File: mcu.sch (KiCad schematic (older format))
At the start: 8 parts

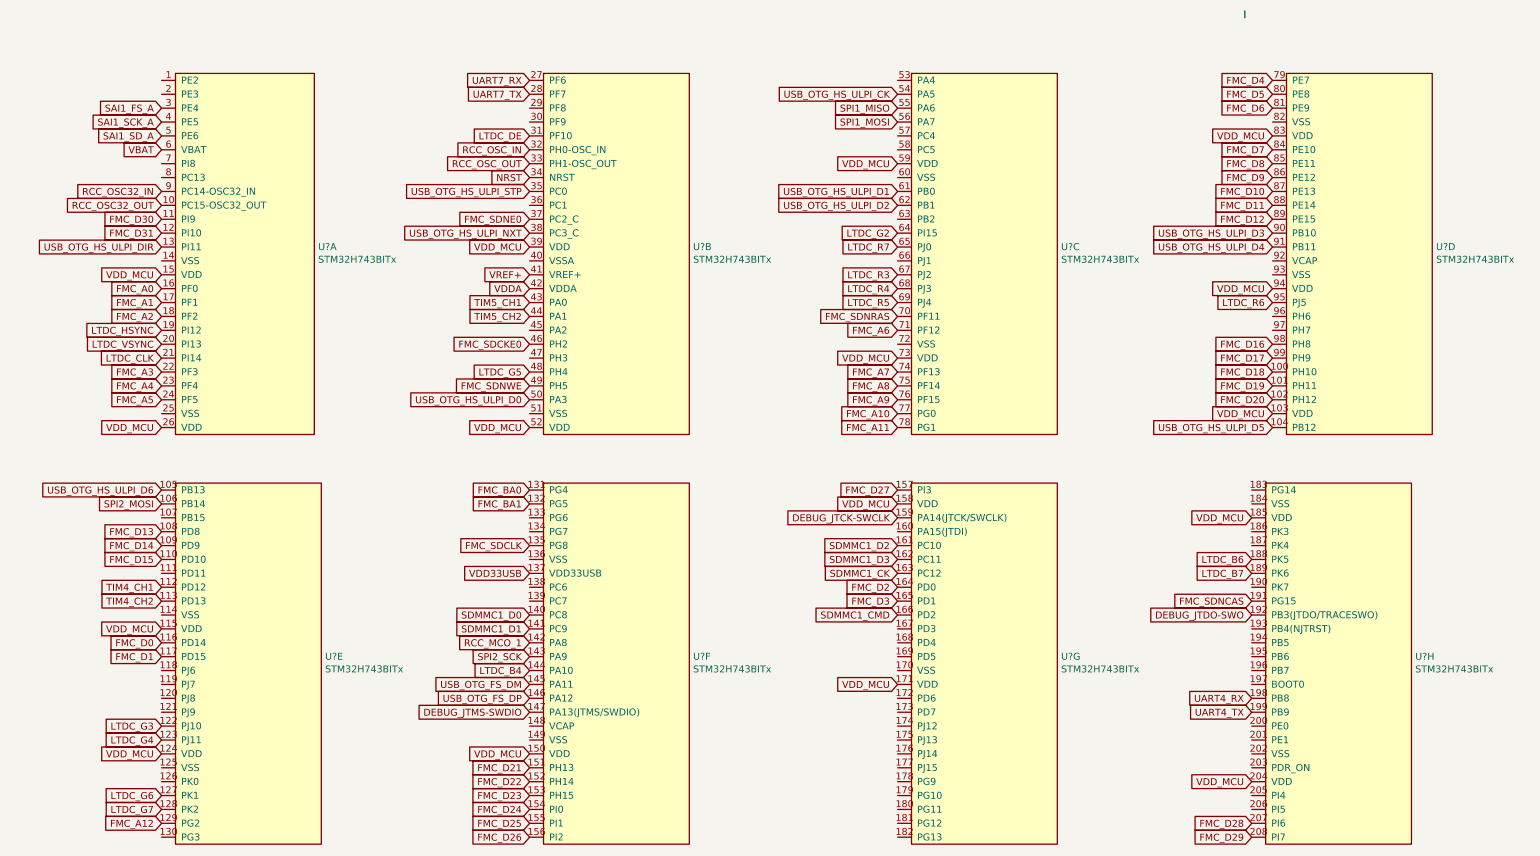
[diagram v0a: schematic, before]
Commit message: Finished MCU power, MCU crystals, started CODEC
Not done CODEC.

Where are the I2S BCLK and LRCLK?
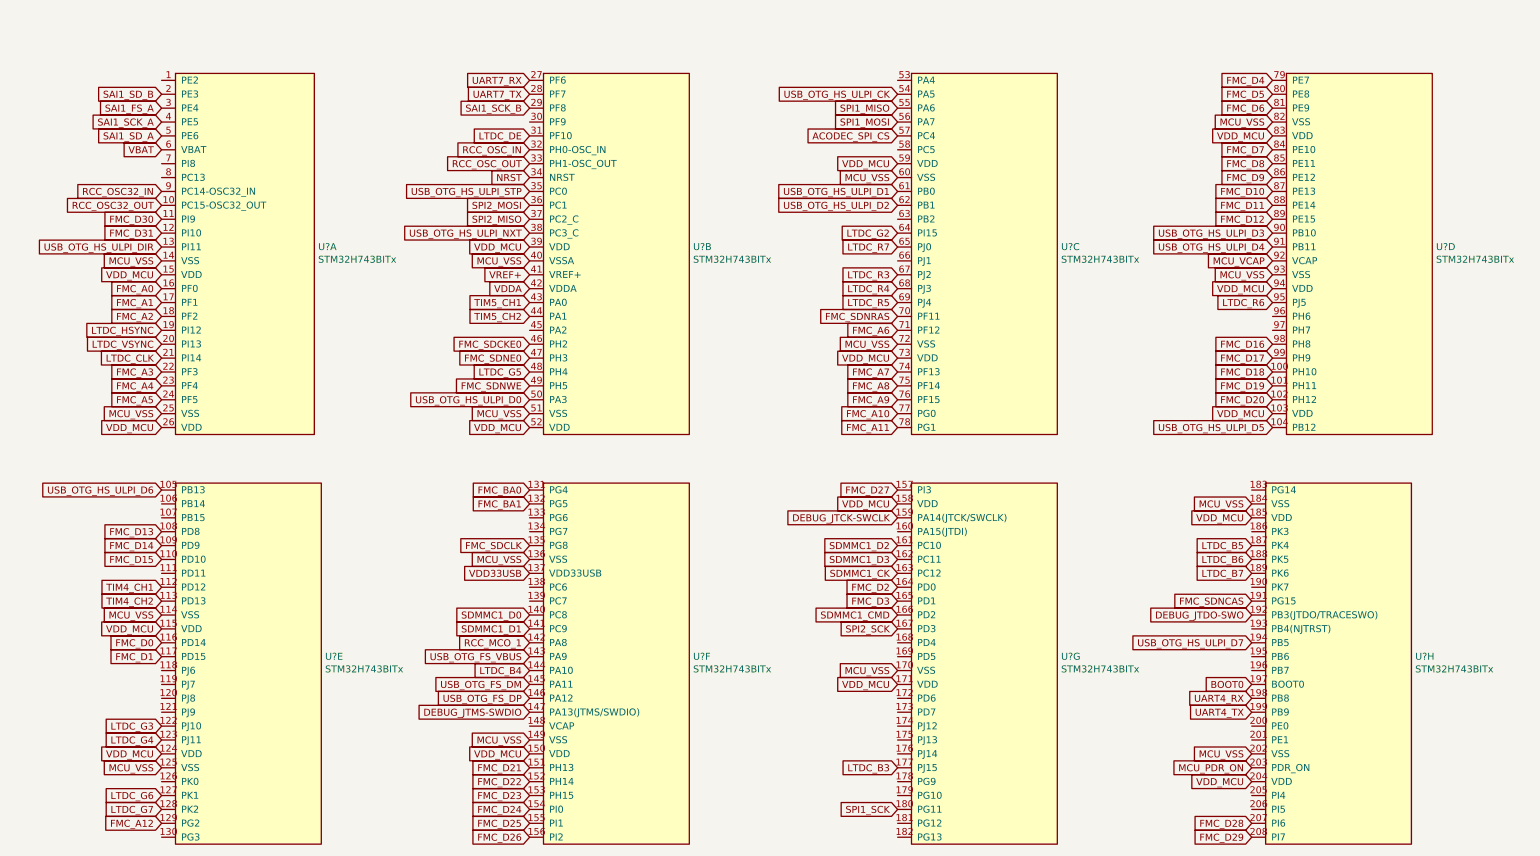
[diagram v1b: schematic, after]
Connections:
- net labels added: ACODEC_SPI_CS, BOOT0, LTDC_B3, LTDC_B5, MCU_PDR_ON, MCU_VCAP, MCU_VSS, SAI1_SCK_B, SAI1_SD_B, SPI1_SCK, SPI2_MISO, USB_OTG_FS_VBUS, USB_OTG_HS_ULPI_D7
- wire segments 1 -> 0
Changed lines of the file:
@@
 $Descr A4 11693 8268
 encoding utf-8
-Sheet 2 3
+Sheet 2 6
 Title ""
 Date ""
@@
 USB_OTG_HS_ULPI_STP
 Text GLabel 4150 1600 0    50   Input ~ 0
-FMC_SDNE0
+SPI2_MISO
 Text GLabel 4150 1700 0    50   Input ~ 0
 USB_OTG_HS_ULPI_NXT
@@
 Text GLabel 1500 3550 0    50   Input ~ 0
 USB_OTG_HS_ULPI_D6
-Text GLabel 1500 3650 0    50   Input ~ 0
-SPI2_MOSI
 Text GLabel 1500 5350 0    50   Input ~ 0
 LTDC_G4
@@
 VDD33USB
 Text GLabel 4150 4750 0    50   Input ~ 0
-SPI2_SCK
+USB_OTG_FS_VBUS
 $Comp
 L midi_studio_components:STM32H743BITx U?
@@
 	1    0    0    -1
 $EndComp
-Wire Wire Line
-	9300 150  9300 100
+Text GLabel 4150 2600 0    50   Input ~ 0
+FMC_SDNE0
+Text GLabel 6800 4550 0    50   Input ~ 0
+SPI2_SCK
+Text GLabel 6800 5550 0    50   Input ~ 0
+LTDC_B3
+Text GLabel 6800 5850 0    50   Input ~ 0
+SPI1_SCK
+Text GLabel 9350 3950 0    50   Input ~ 0
+LTDC_B5
+Text GLabel 9350 4650 0    50   Input ~ 0
+USB_OTG_HS_ULPI_D7
+Text GLabel 9350 4950 0    50   Input ~ 0
+BOOT0
+Text GLabel 4150 1500 0    50   Input ~ 0
+SPI2_MOSI
+Text GLabel 9350 5550 0    50   Input ~ 0
+MCU_PDR_ON
+Text GLabel 1500 1900 0    50   Input ~ 0
+MCU_VSS
+Text GLabel 1500 3000 0    50   Input ~ 0
+MCU_VSS
+Text GLabel 4150 1900 0    50   Input ~ 0
+MCU_VSS
+Text GLabel 4150 3000 0    50   Input ~ 0
+MCU_VSS
+Text GLabel 6800 1300 0    50   Input ~ 0
+MCU_VSS
+Text GLabel 6800 2500 0    50   Input ~ 0
+MCU_VSS
+Text GLabel 9500 900  0    50   Input ~ 0
+MCU_VSS
+Text GLabel 9500 2000 0    50   Input ~ 0
+MCU_VSS
+Text GLabel 1500 4450 0    50   Input ~ 0
+MCU_VSS
+Text GLabel 1500 5550 0    50   Input ~ 0
+MCU_VSS
+Text GLabel 4150 4050 0    50   Input ~ 0
+MCU_VSS
+Text GLabel 4150 5350 0    50   Input ~ 0
+MCU_VSS
+Text GLabel 6800 4850 0    50   Input ~ 0
+MCU_VSS
+Text GLabel 9350 3650 0    50   Input ~ 0
+MCU_VSS
+Text GLabel 9350 5450 0    50   Input ~ 0
+MCU_VSS
+Text GLabel 1500 700  0    50   Input ~ 0
+SAI1_SD_B
+Text GLabel 4150 800  0    50   Input ~ 0
+SAI1_SCK_B
+Text GLabel 9500 1900 0    50   Input ~ 0
+MCU_VCAP
+Text GLabel 6800 1000 0    50   Input ~ 0
+ACODEC_SPI_CS
 $EndSCHEMATC

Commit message: Finished digital part of CODEC
Needed to add SAI2 to get enough pins.
We could have multiplexed all 8 channels on one pin but the SR is limited to
48KHz. I wanted to see how it works with 2 data lines per direction. Then
maximum SR is 96KHz, which we probably won't use but at least its not at the
limit.
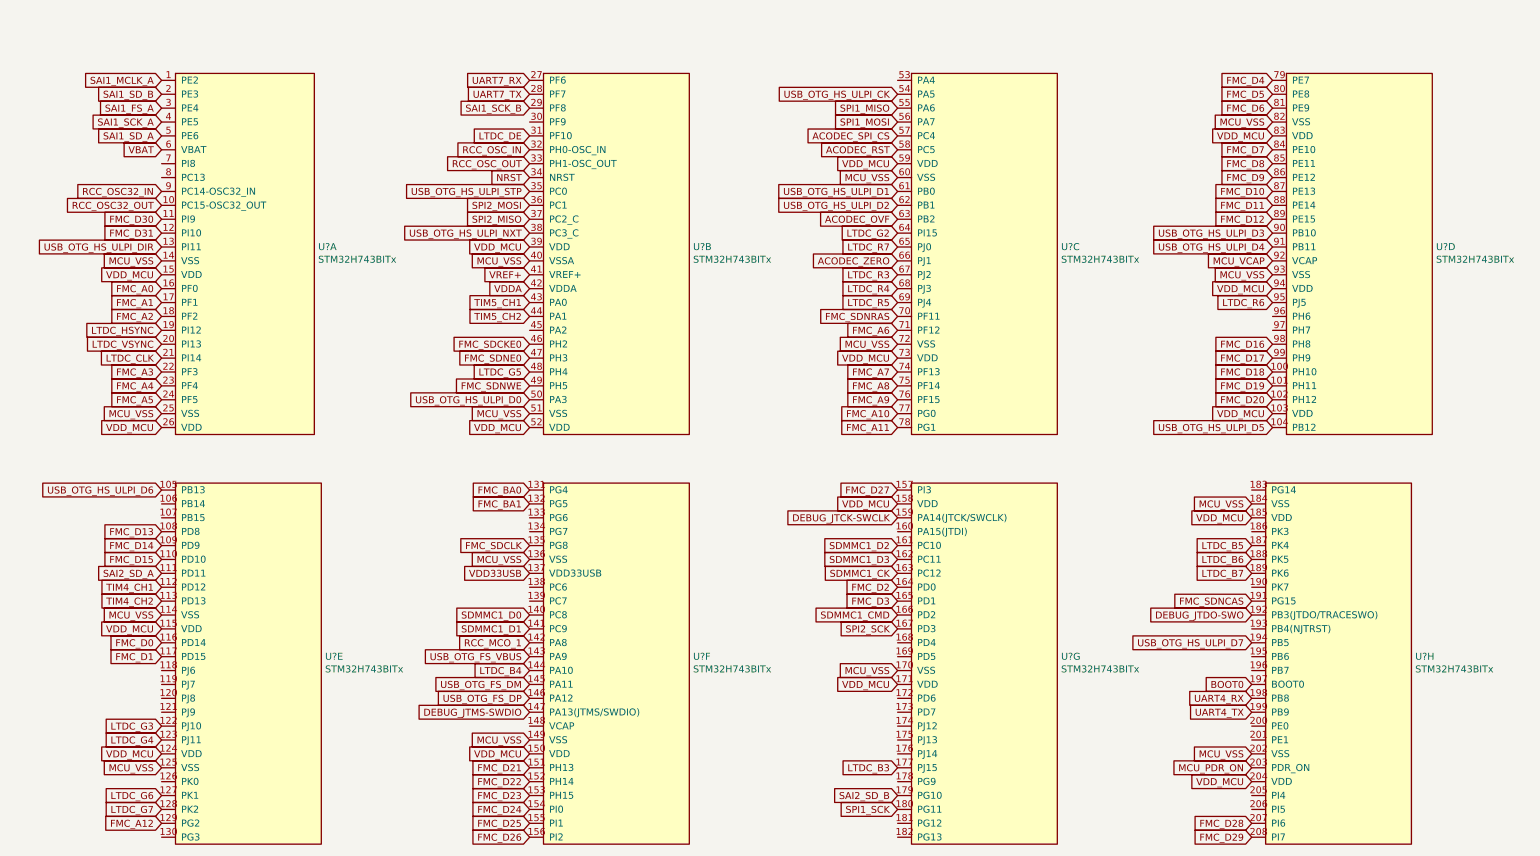
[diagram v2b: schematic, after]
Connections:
- net SAI1_MCLK_A: now reaches U?.1 (PE2)
- net ACODEC_RST: now reaches U?.58 (PC5)
- net ACODEC_OVF: now reaches U?.63 (PB2)
- net ACODEC_ZERO: now reaches U?.66 (PJ1)
- net SAI2_SD_A: now reaches U?.111 (PD11)
- net SAI2_SD_B: now reaches U?.179 (PG10)
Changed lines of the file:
@@
 Text GLabel 6800 1000 0    50   Input ~ 0
 ACODEC_SPI_CS
+Text GLabel 1500 600  0    50   Input ~ 0
+SAI1_MCLK_A
+Text GLabel 1500 4150 0    50   Input ~ 0
+SAI2_SD_A
+Text GLabel 6800 5750 0    50   Input ~ 0
+SAI2_SD_B
+Text GLabel 6800 1100 0    50   Input ~ 0
+ACODEC_RST
+Text GLabel 6800 1600 0    50   Input ~ 0
+ACODEC_OVF
+Text GLabel 6800 1900 0    50   Input ~ 0
+ACODEC_ZERO
 $EndSCHEMATC

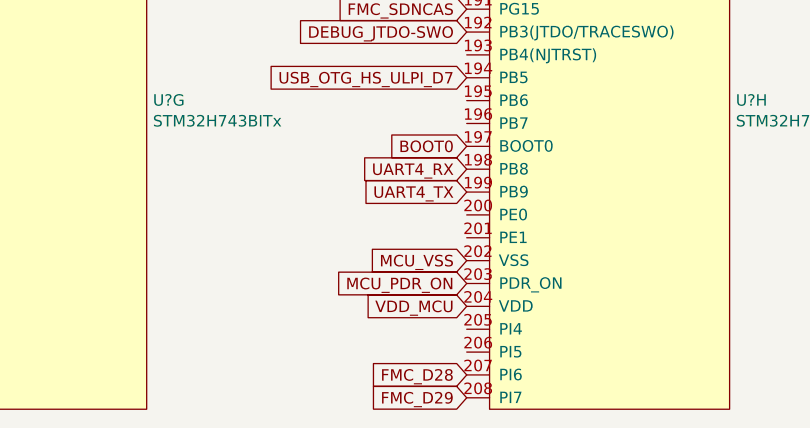
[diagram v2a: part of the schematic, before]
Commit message: Added SDRAM to schematic
We're assuming we use a unique NBLx for each chip because it seems like if you
actually had a chip with a 32-bit wide data bus, it would have 4 DQM (NBL) pins.
So in this way we simulate a 32-bit wide data bus.
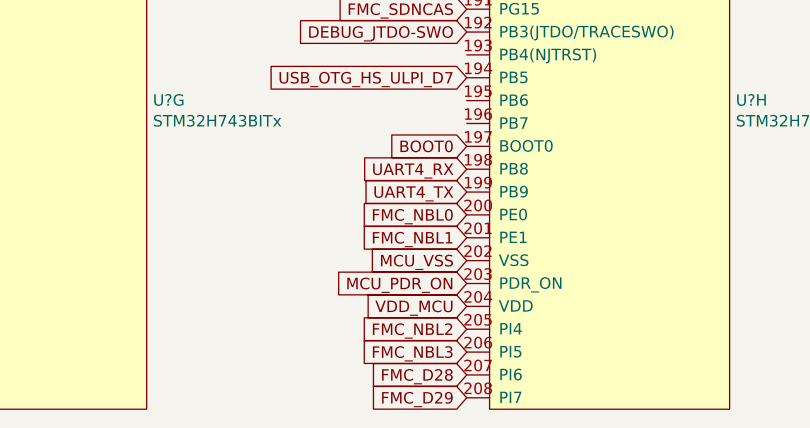
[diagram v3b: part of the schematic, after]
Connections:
- net FMC_NBL0: now reaches U?.200 (PE0)
- net FMC_NBL1: now reaches U?.201 (PE1)
- net FMC_NBL2: now reaches U?.205 (PI4)
- net FMC_NBL3: now reaches U?.206 (PI5)
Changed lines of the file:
@@
 $Descr A4 11693 8268
 encoding utf-8
-Sheet 2 6
+Sheet 2 7
 Title ""
 Date ""
@@
 Text GLabel 6800 1900 0    50   Input ~ 0
 ACODEC_ZERO
+Text GLabel 9350 5250 0    50   Input ~ 0
+FMC_NBL0
+Text GLabel 9350 5350 0    50   Input ~ 0
+FMC_NBL1
+Text GLabel 9350 5750 0    50   Input ~ 0
+FMC_NBL2
+Text GLabel 9350 5850 0    50   Input ~ 0
+FMC_NBL3
 $EndSCHEMATC

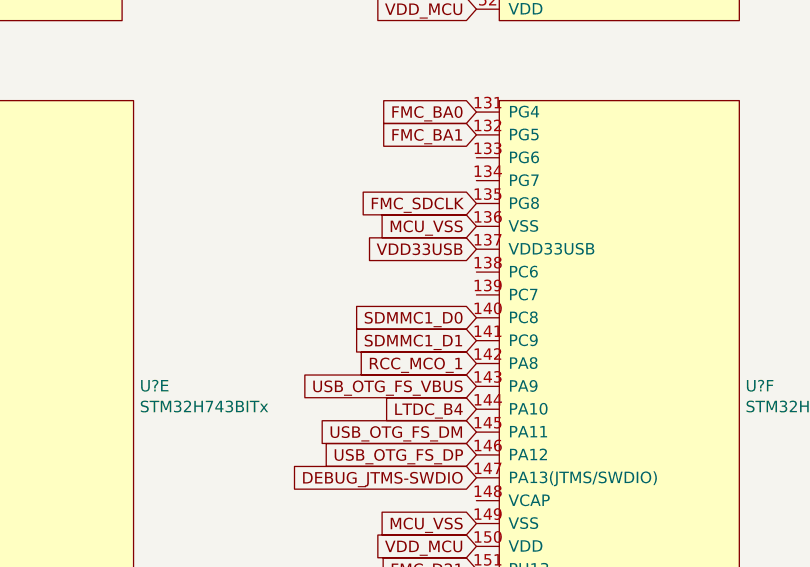
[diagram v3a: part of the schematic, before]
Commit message: Added SD card.
Working on LCD screen. Not yet finished.
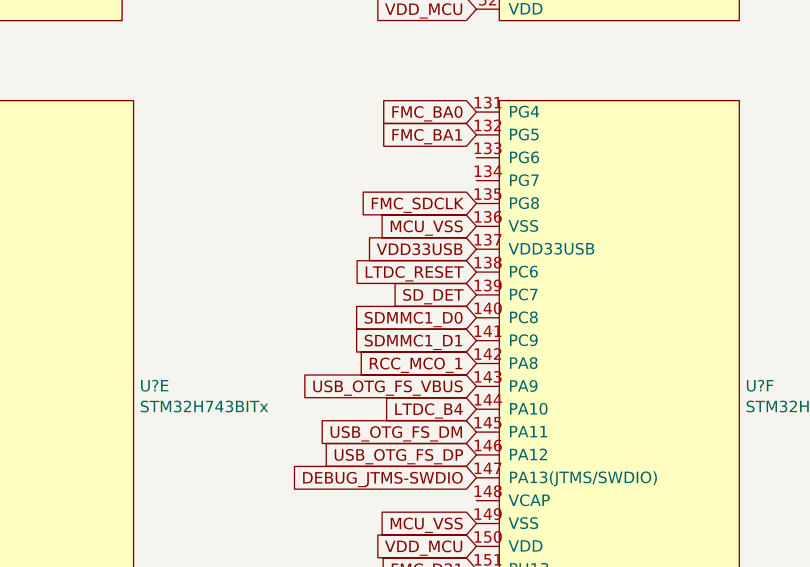
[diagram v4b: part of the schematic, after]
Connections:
- net LTDC_RESET: now reaches U?.138 (PC6)
- net SD_DET: now reaches U?.139 (PC7)
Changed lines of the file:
@@
 $Descr A4 11693 8268
 encoding utf-8
-Sheet 2 7
+Sheet 2 9
 Title ""
 Date ""
@@
 Text GLabel 9350 5850 0    50   Input ~ 0
 FMC_NBL3
+Text GLabel 4150 4350 0    50   Input ~ 0
+SD_DET
+Text GLabel 4150 4250 0    50   Input ~ 0
+LTDC_RESET
 $EndSCHEMATC
